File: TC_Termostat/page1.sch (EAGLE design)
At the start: 30 parts, among them IC1 F20X3---N14, P1_1 SOLDER_POINTA, P1_2 SOLDER_POINTA, P1_4 SOLDER_POINTA, P1_5 SOLDER_POINTA, P1_6 SOLDER_POINTA, P1_7 SOLDER_POINTA, P2_7 SOLDER_POINTA, Q1 2N2219A, X1 J_PROG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

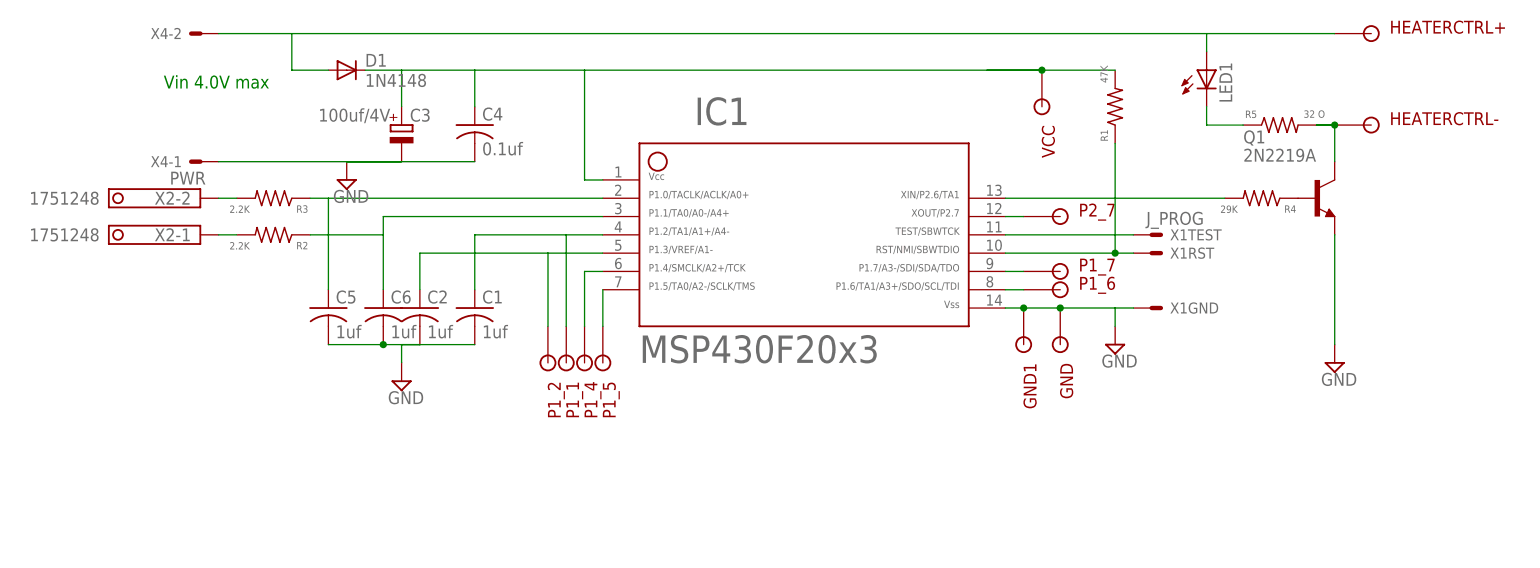
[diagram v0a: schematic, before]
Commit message: Added revised Schematic  for TC-Thermostat
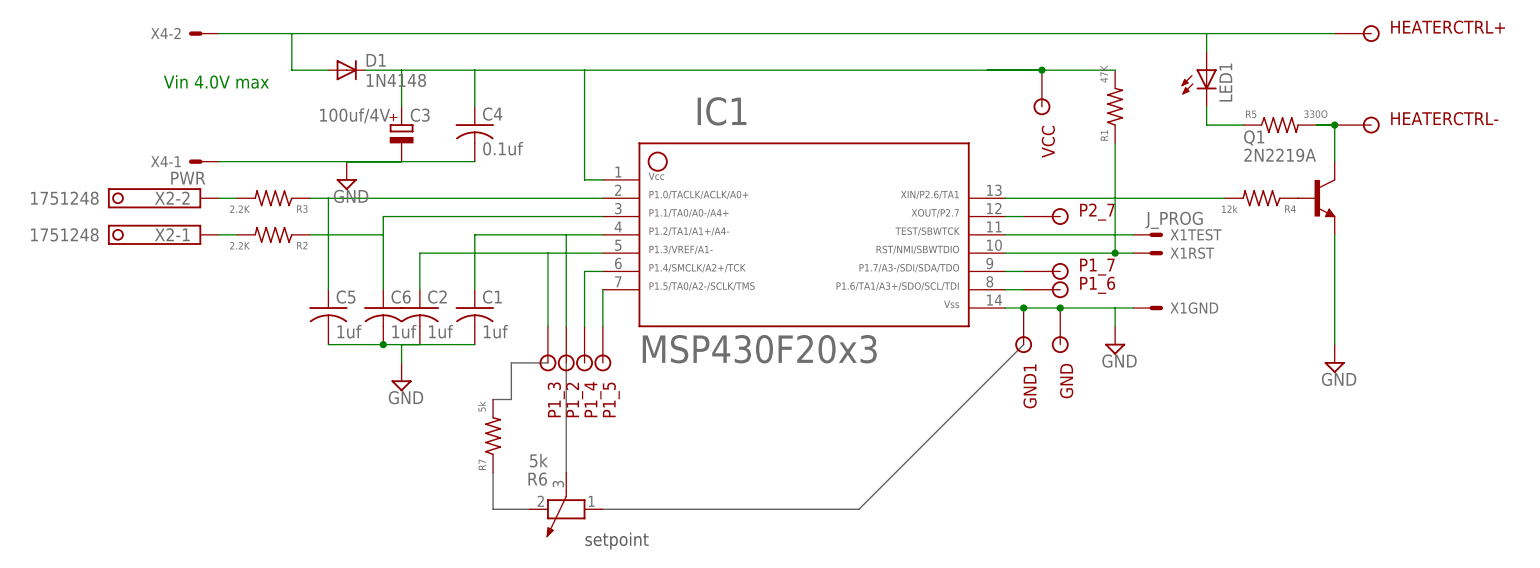
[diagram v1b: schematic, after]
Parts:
- removed P1_1: SOLDER_POINTA, Stofer:SOLDER_POINTA
- added P1_3: SOLDER_POINTA, Stofer:SOLDER_POINTA
- added R6: 5k, rcl:POTENTIOMETER_PT-10
- added R7: 5k, rcl:R-US_0207/15
- R4: value 29K -> 12k
- R5: value 32 O -> 330O
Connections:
- net N$7: now also P1_3.P$1; no longer P1_2.P$1
- net N$9: now also P1_2.P$1; no longer P1_1.P$1
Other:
- note added: "setpoint"
- moved on the sheet: P1_2
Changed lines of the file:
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@@
 <part name="V4" library="supply2" deviceset="GND" device=""/>
 <part name="Q1" library="transistor-npn" deviceset="2N2219A" device="TO92_EBC" value="2N2219A"/>
-<part name="R4" library="rcl" deviceset="R-US_" device="M0805" value="29K"/>
+<part name="R4" library="rcl" deviceset="R-US_" device="M0805" value="12k"/>
 <part name="V3" library="supply2" deviceset="GND" device=""/>
 <part name="HEATERCTRL-" library="Stofer" deviceset="SOLDER_POINT" device="A"/>
 <part name="HEATERCTRL+" library="Stofer" deviceset="SOLDER_POINT" device="A"/>
 <part name="LED1" library="led" deviceset="LED" device="5MM"/>
-<part name="R5" library="rcl" deviceset="R-US_" device="0207/15" value="32 O"/>
+<part name="R5" library="rcl" deviceset="R-US_" device="0207/15" value="330O"/>
 <part name="P1_5" library="Stofer" deviceset="SOLDER_POINT" device="A"/>
 <part name="P1_4" library="Stofer" deviceset="SOLDER_POINT" device="A"/>
@@
 <part name="D1" library="dedenbear" deviceset="1N4148" device=""/>
 <part name="C5" library="rcl" deviceset="C-US" device="C0805" value="1uf"/>
-<part name="P1_1" library="Stofer" deviceset="SOLDER_POINT" device="A"/>
 <part name="P1_2" library="Stofer" deviceset="SOLDER_POINT" device="A"/>
+<part name="P1_3" library="Stofer" deviceset="SOLDER_POINT" device="A"/>
 <part name="C6" library="rcl" deviceset="C-US" device="C0805" value="1uf"/>
 <part name="X2" library="con-phoenix-350" deviceset="1751248" device=""/>
+<part name="R6" library="rcl" deviceset="POTENTIOMETER_" device="PT-10" value="5k"/>
+<part name="R7" library="rcl" deviceset="R-US_" device="0207/15" value="5k"/>
 </parts>
 <sheets>
@@
 <plain>
 <text x="-50.8" y="55.88" size="1.778" layer="91">Vin 4.0V max </text>
+<wire x1="-2.54" y1="12.7" x2="-2.54" y2="17.78" width="0.1524" layer="97"/>
+<wire x1="-2.54" y1="17.78" x2="2.54" y2="17.78" width="0.1524" layer="97"/>
+<wire x1="-5.08" y1="2.54" x2="-5.08" y2="-2.54" width="0.1524" layer="97"/>
+<wire x1="-5.08" y1="-2.54" x2="0" y2="-2.54" width="0.1524" layer="97"/>
+<wire x1="10.16" y1="-2.54" x2="45.72" y2="-2.54" width="0.1524" layer="97"/>
+<wire x1="45.72" y1="-2.54" x2="68.58" y2="20.32" width="0.1524" layer="97"/>
+<wire x1="5.08" y1="17.78" x2="5.08" y2="2.54" width="0.1524" layer="97"/>
+<text x="7.62" y="-7.62" size="1.778" layer="97">setpoint</text>
+<wire x1="-5.08" y1="12.7" x2="-2.54" y2="12.7" width="0.1524" layer="97"/>
 </plain>
 <instances>
@@
 <instance part="D1" gate="G$1" x="-22.86" y="58.42"/>
 <instance part="C5" gate="G$1" x="-27.94" y="25.4"/>
-<instance part="P1_1" gate="G$1" x="5.08" y="12.7" rot="R270"/>
-<instance part="P1_2" gate="G$1" x="2.54" y="12.7" rot="R270"/>
+<instance part="P1_2" gate="G$1" x="5.08" y="12.7" rot="R270"/>
+<instance part="P1_3" gate="G$1" x="2.54" y="12.7" rot="R270"/>
 <instance part="C6" gate="G$1" x="-20.32" y="25.4"/>
 <instance part="X2" gate="-1" x="-45.72" y="35.56" rot="R180"/>
 <instance part="X2" gate="-2" x="-45.72" y="40.64" rot="R180"/>
+<instance part="R6" gate="1" x="5.08" y="-2.54" rot="R180"/>
+<instance part="R7" gate="G$1" x="-5.08" y="7.62" rot="R90"/>
 </instances>
 <busses>
@@
 <pinref part="IC1" gate="G$1" pin="5"/>
 <pinref part="C2" gate="G$1" pin="1"/>
-<pinref part="P1_2" gate="G$1" pin="P$1"/>
+<pinref part="P1_3" gate="G$1" pin="P$1"/>
 <wire x1="2.54" y1="22.86" x2="2.54" y2="33.02" width="0.1524" layer="91"/>
 </segment>
@@
 <pinref part="C1" gate="G$1" pin="1"/>
 <pinref part="IC1" gate="G$1" pin="4"/>
-<pinref part="P1_1" gate="G$1" pin="P$1"/>
+<pinref part="P1_2" gate="G$1" pin="P$1"/>
 <wire x1="5.08" y1="35.56" x2="10.16" y2="35.56" width="0.1524" layer="91"/>
 <wire x1="5.08" y1="22.86" x2="5.08" y2="35.56" width="0.1524" layer="91"/>
